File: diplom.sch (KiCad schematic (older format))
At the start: 124 parts, among them J1 USB_B, J2 Barrel_Jack, J3 USB_B, J4 Screw_Terminal_01x03, J5 Screw_Terminal_01x04, J6 Screw_Terminal_01x04, J7 Screw_Terminal_01x04, J8 Screw_Terminal_01x02, Q1 S8050, SW1 SW_Push, SW2 SW_SPST, SW3 SW_SPDT, SW4 SW_SPDT, SW5 SW_Push, SW6 SW_Push, SW7 SW_Push, SW8 SW_Push, U1 LD3985M33R, U10 L298, U11 LS7366R, U12 LS7366R, U2 TPS54620, U3 STM32F103_STLINK, U4 CP2102, U5 TPS76833, U6 STM32F446, U7 STM32F103_DC, U8 TCA9517, U9 PCF8574, Y1 8MHz, Y2 8MHz, Y3 20MHz, Y4 20MHz

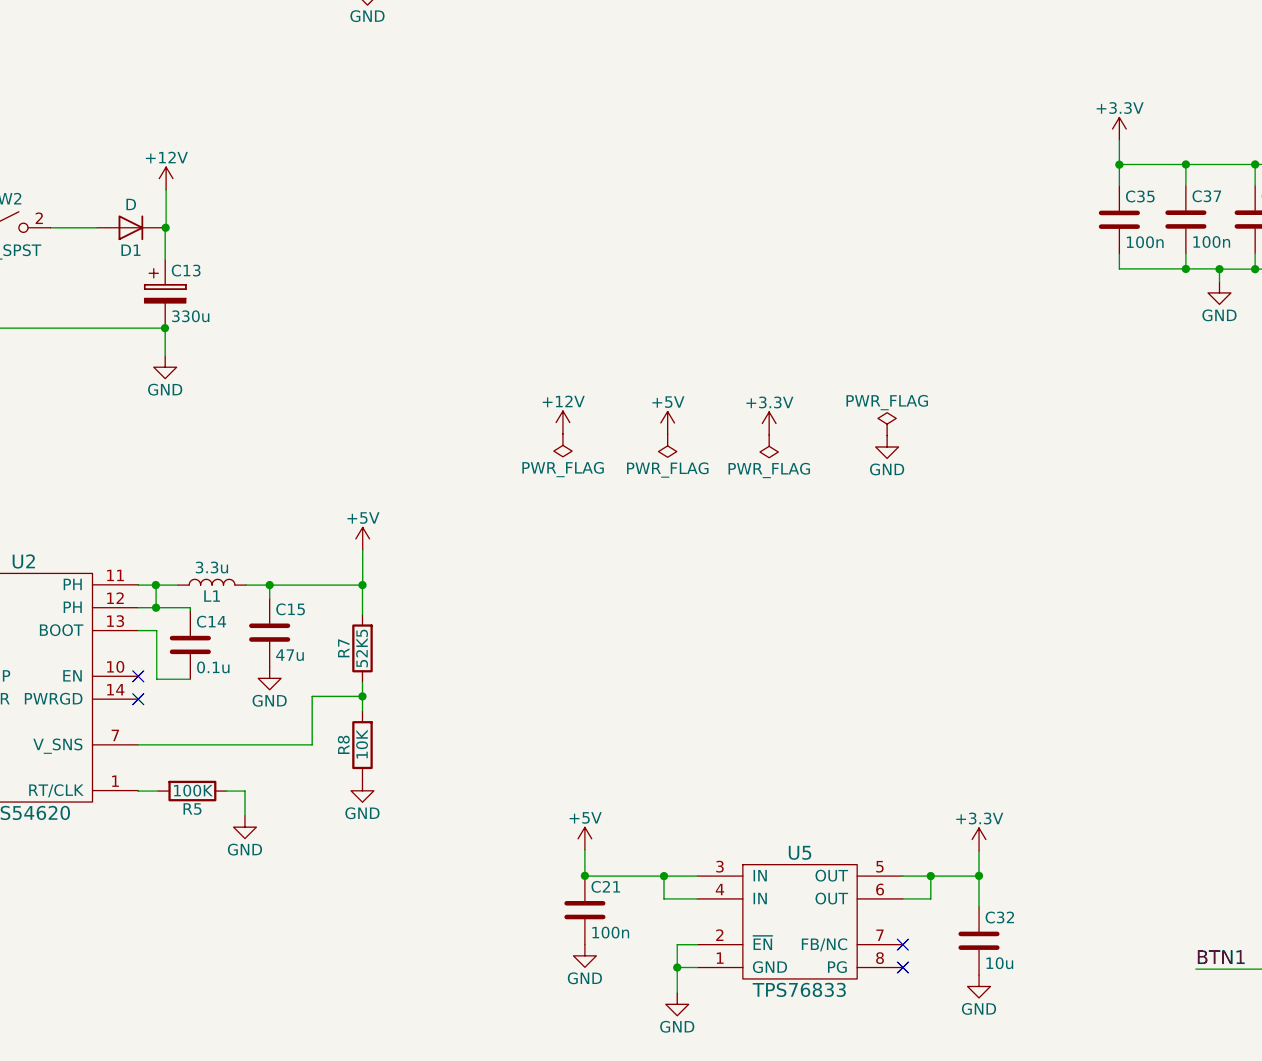
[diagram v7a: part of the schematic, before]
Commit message: PCB routing started. Quartz footprint changed
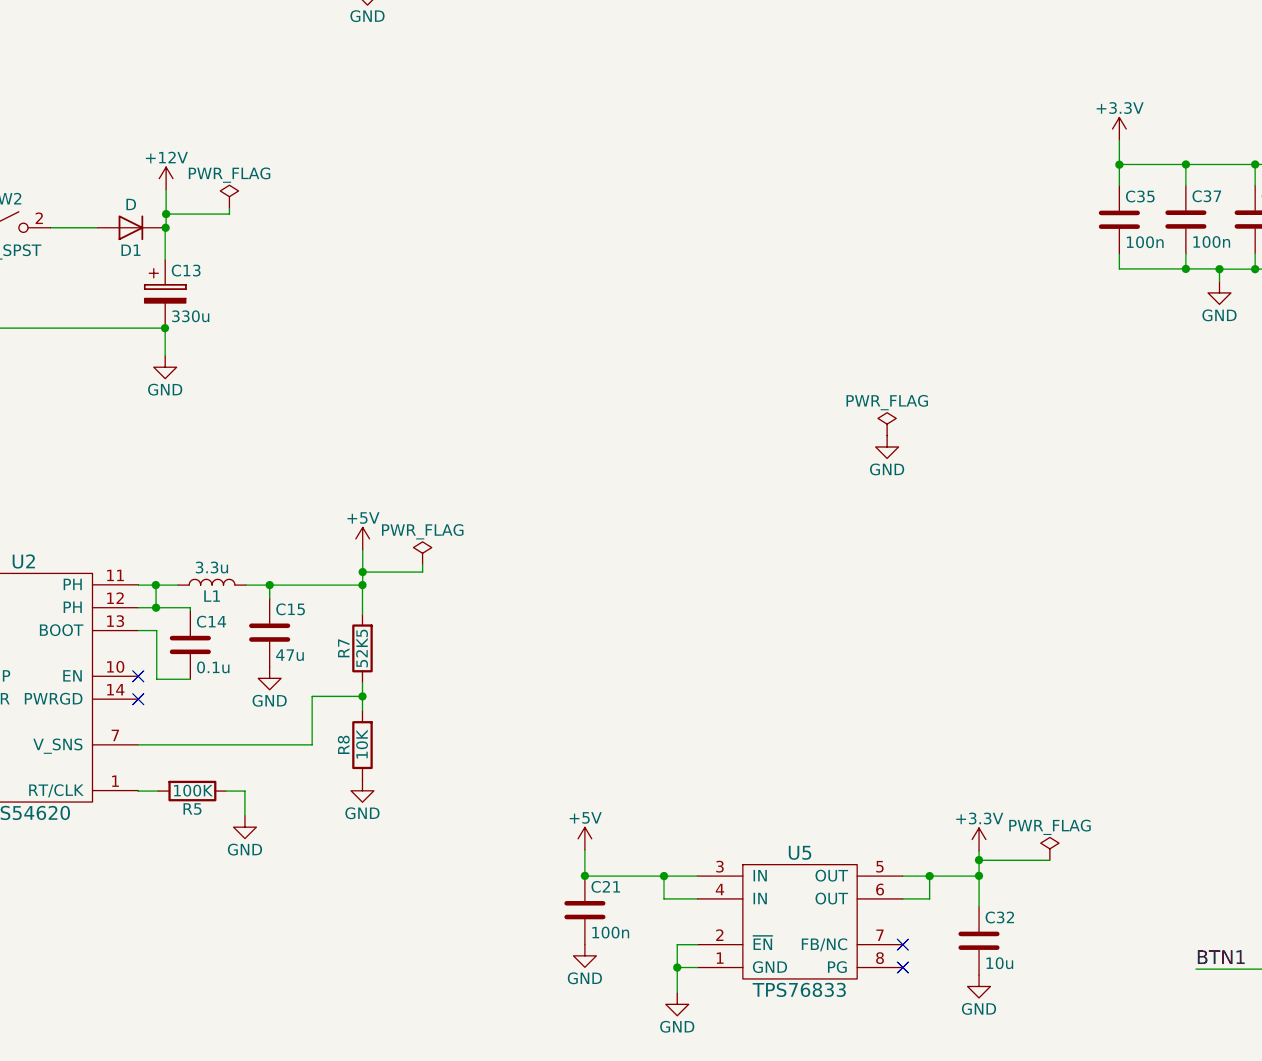
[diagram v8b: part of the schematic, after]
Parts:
- Y1, Y2, Y3, Y4: footprint Crystals:Crystal_SMD_HC49-SD_HandSoldering -> Crystals:Crystal_SMD_EuroQuartz_MQ2-2pin_7.0x5.0mm_HandSoldering
